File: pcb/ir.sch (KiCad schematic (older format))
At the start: 0 parts

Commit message: IR matrix complete minus control transistor
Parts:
- added Q?: 2N7002, Package_TO_SOT_SMD:SOT-23, symbol Transistor_FET:2N7002
- added R?: 150, symbol Device:R
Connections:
- net labels added: +12V, GND, IR_OUT, IR_OUT0, IR_OUT1, IR_OUT2, IR_OUT3, IR_OUT4, IR_OUT5, IR_OUT6, en
- net labels removed: IR_col, IR_row0, IR_row1, IR_row2, IR_row3, IR_row4, IR_row5, IR_row6
- wire segments 10 -> 53

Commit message: MOSFET model added
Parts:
- removed Q?: 2N7002, Package_TO_SOT_SMD:SOT-23, symbol Transistor_FET:2N7002
- added Q?: AO3400, Package_TO_SOT_SMD:SOT-23, symbol rasbot:AO3400
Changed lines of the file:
@@
-$EndComp
-$Comp
-L Transistor_FET:2N7002 Q?
-U 1 1 5D41DADF
-P 2650 7200
-F 0 "Q?" H 2856 7246 50  0000 L CNN
-F 1 "2N7002" H 2856 7155 50  0000 L CNN
-F 2 "Package_TO_SOT_SMD:SOT-23" H 2850 7125 50  0001 L CIN
-F 3 "https://www.fairchildsemi.com/datasheets/2N/2N7002.pdf" H 2650 7200 50  0001 L CNN
-	1    2650 7200
-	1    0    0    -1
 $EndComp
 $Comp
@@
 Wire Bus Line
 	2400 1150 2400 6300
+$Comp
+L rasbot:AO3400 Q?
+U 1 1 5D362773
+P 2700 7200
+F 0 "Q?" H 2856 7246 50  0000 L CNN
+F 1 "AO3400" H 2856 7155 50  0000 L CNN
+F 2 "Package_TO_SOT_SMD:SOT-23" H 3425 7125 50  0001 C CNN
+F 3 "http://dalincom.ru/datasheet/AO3400.pdf" H 2700 7200 50  0001 C CNN
+	1    2700 7200
+	1    0    0    -1
+$EndComp
 $EndSCHEMATC

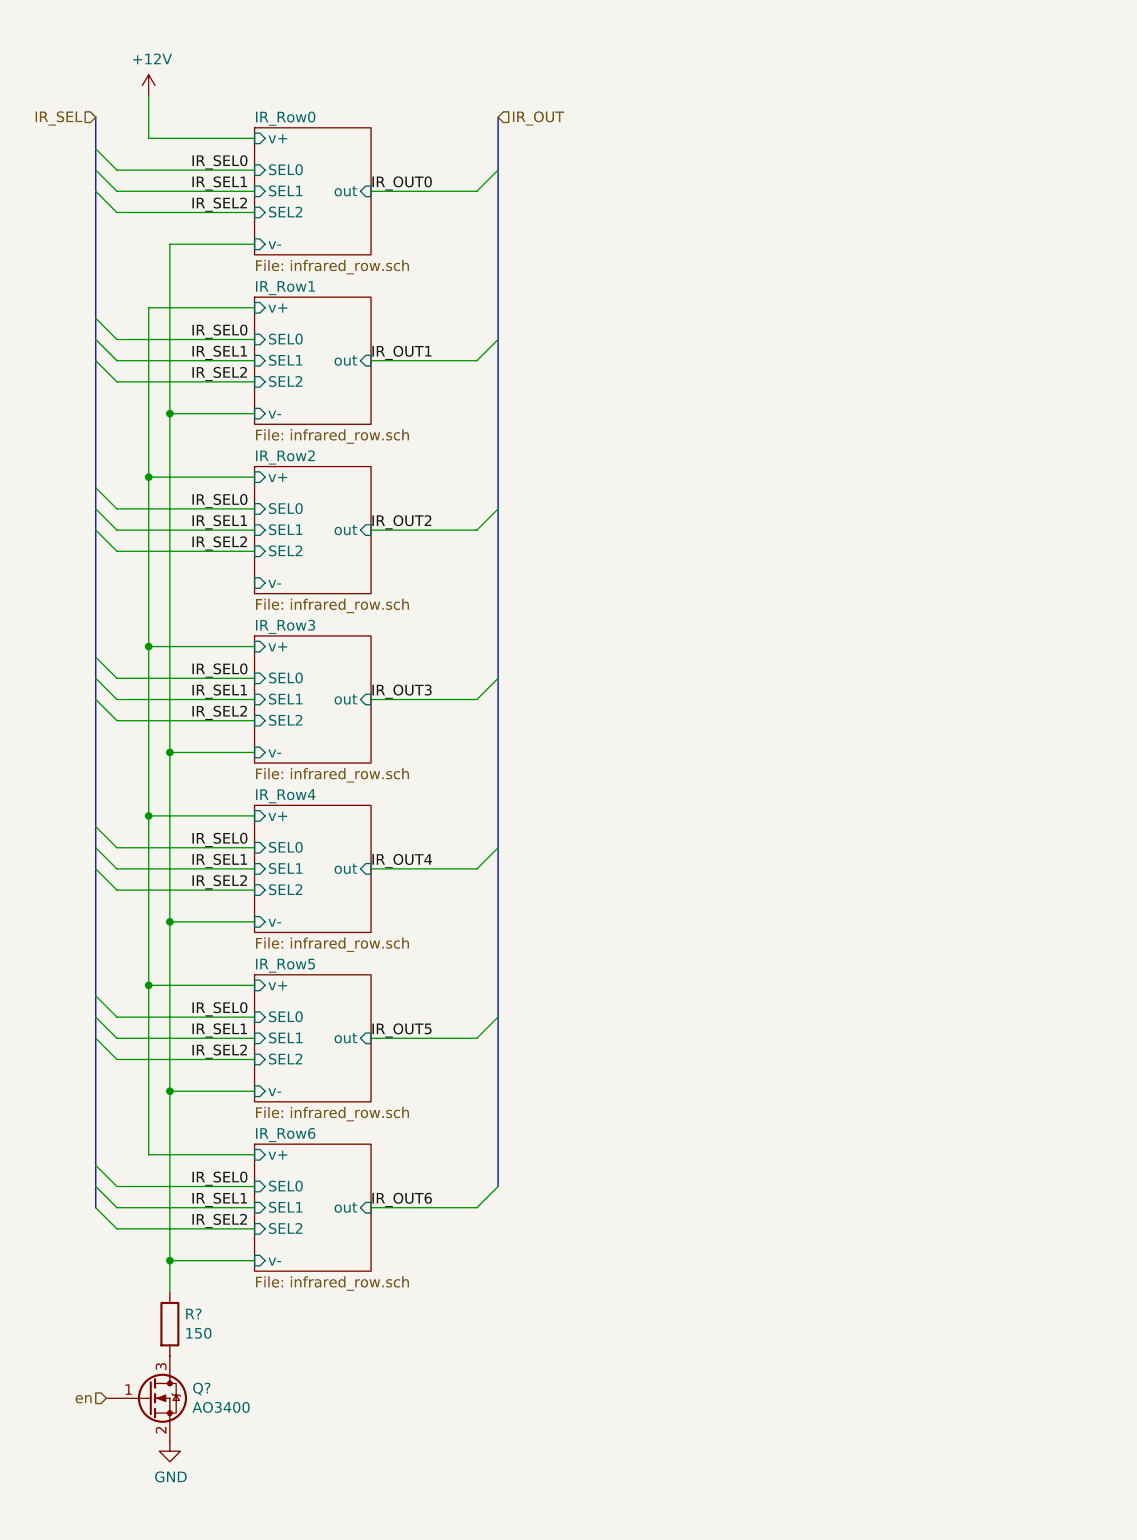
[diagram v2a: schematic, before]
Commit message: IR Matrix - Missing Supply Connection
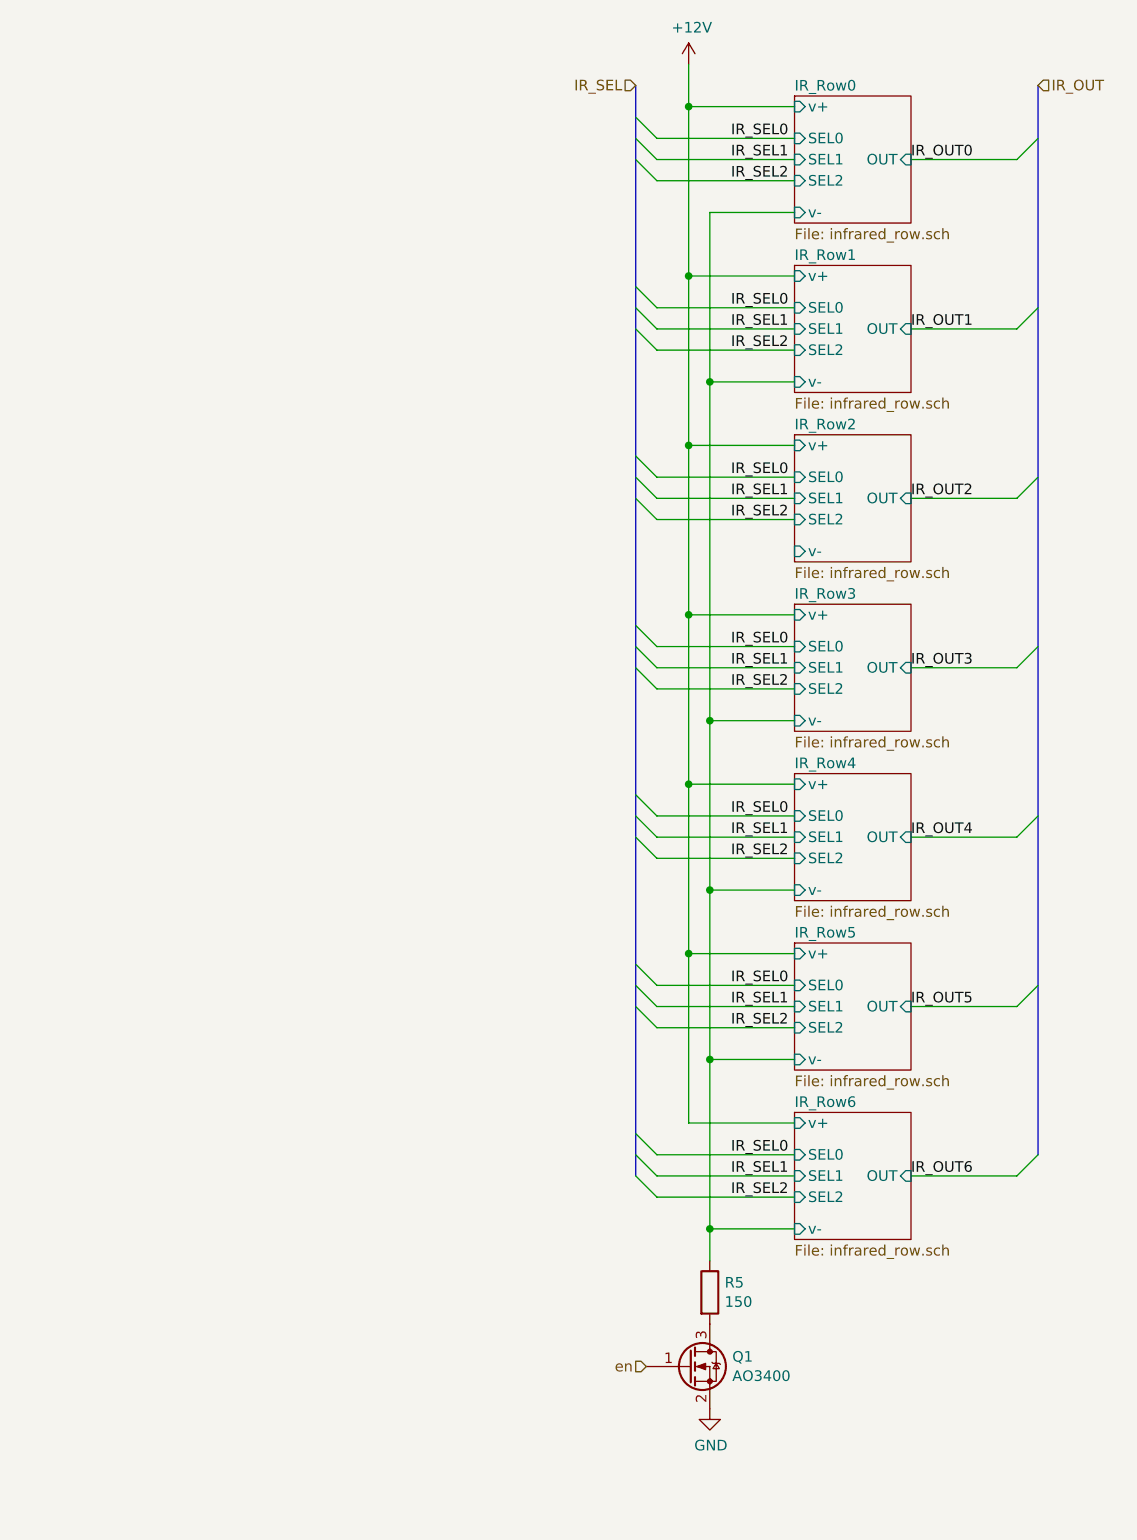
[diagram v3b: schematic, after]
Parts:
- gave numbers to parts that had none: 2
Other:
- moved on the sheet: Q1, R5

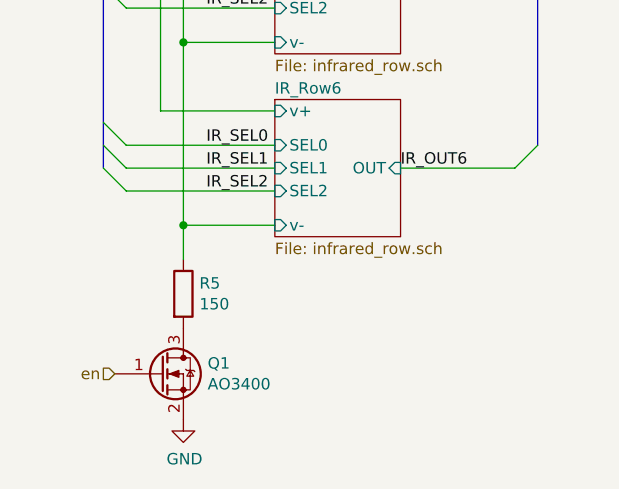
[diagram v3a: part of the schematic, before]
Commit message: STM32F407 and JLink
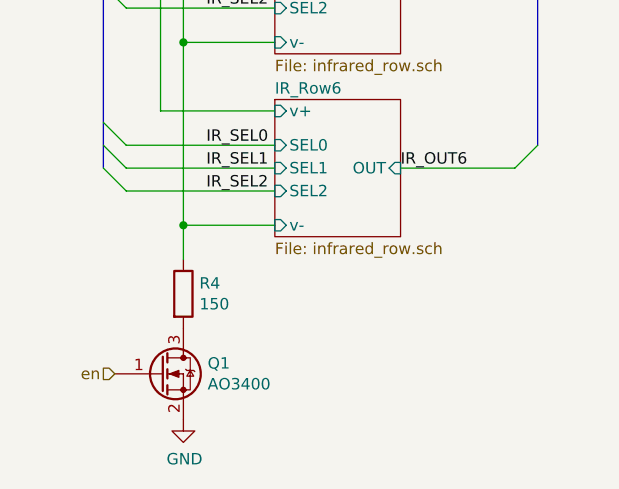
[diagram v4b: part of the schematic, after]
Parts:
- renumbered R5 to R4
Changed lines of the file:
@@
 	5050 1450 5700 1450
 $Comp
-L power:+12V #PWR0101
+L power:+12V #PWR020
 U 1 1 5D40BFEA
 P 5200 900
-F 0 "#PWR0101" H 5200 750 50  0001 C CNN
+F 0 "#PWR020" H 5200 750 50  0001 C CNN
 F 1 "+12V" H 5215 1073 50  0000 C CNN
 F 2 "" H 5200 900 50  0001 C CNN
@@
 IR_OUT6
 $Comp
-L Device:R R5
+L Device:R R4
 U 1 1 5D41D265
 P 5300 6700
-F 0 "R5" H 5370 6746 50  0000 L CNN
+F 0 "R4" H 5370 6746 50  0000 L CNN
 F 1 "150" H 5370 6655 50  0000 L CNN
 F 2 "" V 5230 6700 50  0001 C CNN
@@
 $EndComp
 $Comp
-L power:GND #PWR0102
+L power:GND #PWR021
 U 1 1 5D41F6C3
 P 5300 7250
-F 0 "#PWR0102" H 5300 7000 50  0001 C CNN
+F 0 "#PWR021" H 5300 7000 50  0001 C CNN
 F 1 "GND" H 5305 7077 50  0000 C CNN
 F 2 "" H 5300 7250 50  0001 C CNN

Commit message: Connect IR Matrix to MCU
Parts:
- R4: footprint (none) -> Resistor_SMD:R_0805_2012Metric
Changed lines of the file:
@@
 F 0 "R4" H 5370 6746 50  0000 L CNN
 F 1 "150" H 5370 6655 50  0000 L CNN
-F 2 "" V 5230 6700 50  0001 C CNN
+F 2 "Resistor_SMD:R_0805_2012Metric" V 5230 6700 50  0001 C CNN
 F 3 "~" H 5300 6700 50  0001 C CNN
 	1    5300 6700
